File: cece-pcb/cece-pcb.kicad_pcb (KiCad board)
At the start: 2 copper layers, 57 x 80.5 mm, 51 parts, among them J1 SERIAL, J2 HTU21D, J3 Li-Ion Battery, J4 VAC, K1 SANYOU_SRD_Form_C, Q1 Q_NPN, Q2 Q_NPN, SW1 RES, U1 ESP-12F, U2 MCP73811T-420I-OT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

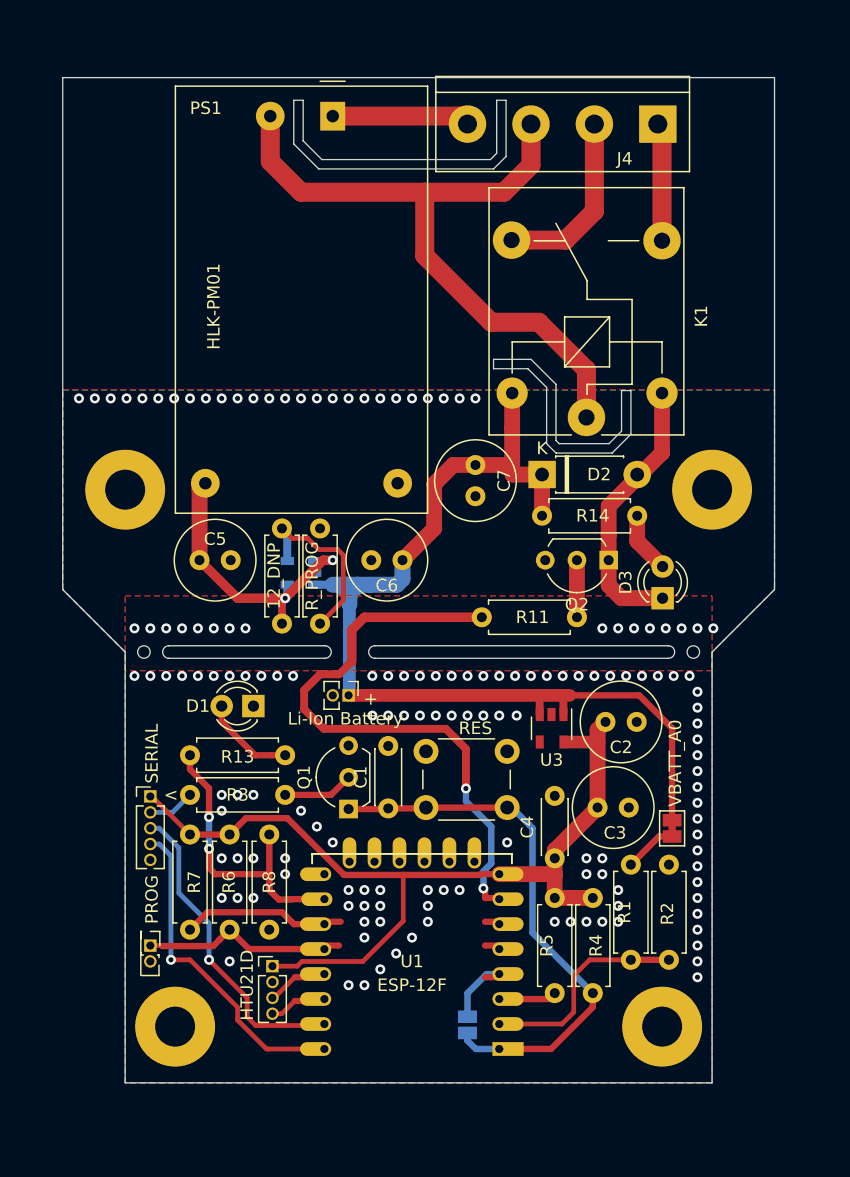
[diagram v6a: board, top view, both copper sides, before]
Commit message: Add jumper to send 5V directly to the LDO if no battery is installed
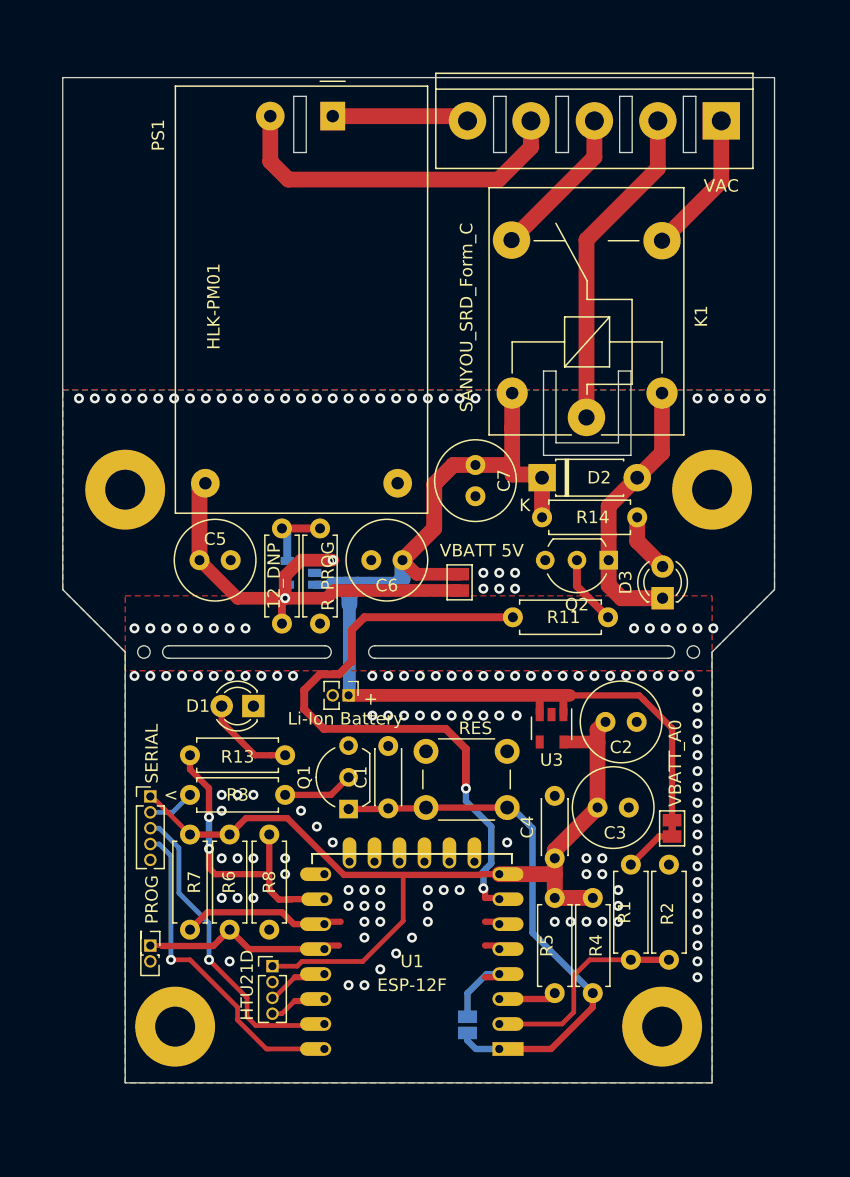
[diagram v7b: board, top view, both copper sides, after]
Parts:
- added JP3: VBATT 5V, Jumper:SolderJumper-2_P1.3mm_Open_Pad1.0x1.5mm, F.Cu at (144.8, 74.4)
- J4: footprint TerminalBlock:TerminalBlock_bornier-4_P5.08mm -> TerminalBlock:TerminalBlock_bornier-5_P5.08mm
- moved R10 7.62 mm to (133.6, 70.1), turned to 270 degrees
- moved J4 5.09 mm to (165.7, 37.5)
- moved R11 2.49 mm to (156.7, 77.2)
- moved D2 0.25 mm to (151.4, 66.0)
- moved R14 0.13 mm to (159.0, 69.2)
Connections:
- J4 pad 2: /NC -> /C
- J4 pad 3: /C -> /NC
- J4 pad 4: /LN -> /ACN
- NT1 pad 1: /ESP-12_common/D0 -> (no net)
- NT2 pad 1: /ESP-12_common/D5|SCK -> (no net)
- NT3 pad 1: /ESP-12_common/D6|MISO -> (no net)
- NT8 pad 2: /ESP-12_common/D3 -> (no net)
- NT9 pad 2: /ESP-12_common/D4 -> (no net)
- PS1 pad 1: /LN -> /ACL
- PS1 pad 2: /C -> /ACN
- U1 pad 17: Net-(U1-Pad17) -> (no net)
- U1 pad 18: Net-(U1-Pad18) -> (no net)
- U1 pad 19: Net-(U1-Pad19) -> (no net)
- U1 pad 20: Net-(U1-Pad20) -> (no net)
- U1 pad 21: Net-(U1-Pad21) -> (no net)
- U1 pad 22: Net-(U1-Pad22) -> (no net)
- U3 pad 4: Net-(U3-Pad4) -> (no net)
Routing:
- net /C: track 55.4 -> 26.1 mm
- net /ACN: track 0.00 -> 28.3 mm
- net +5V: track 24.7 -> 39.9 mm
- net /LN: track 11.1 -> 0.00 mm
- net /ACL: track 0.00 -> 11.0 mm
- net Net-(R10-Pad1): track 15.4 -> 6.39 mm
- net +BATT: track 84.3 -> 89.4 mm
- net /RLY: track 47.1 -> 49.5 mm
- net /NC: track 14.6 -> 12.3 mm
- net /NO: track 9.48 -> 11.6 mm
- net Net-(Q2-Pad2): track 4.57 -> 5.60 mm
- net GND: vias 150 -> 159
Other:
- outline, holes or cut-outs redrawn
- board text added: "L"
- board text added: "N"
- board text removed: "L/N"
